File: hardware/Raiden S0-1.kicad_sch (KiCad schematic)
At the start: 42 parts, among them J1 Conn_01x15, J2 Conn_01x15, J4 Conn_02x03_Counter_Clockwise, J5 Conn_02x02_Counter_Clockwise, J6 Conn_02x02_Counter_Clockwise, P1 USB_C_Receptacle_USB2.0_14P, SW1 SW_Push, SW2 SW_Push, U1 ESP32-S3FN8, U2 AZ1117C-3.3, Y1 32.768kHz, Y2 40MHz

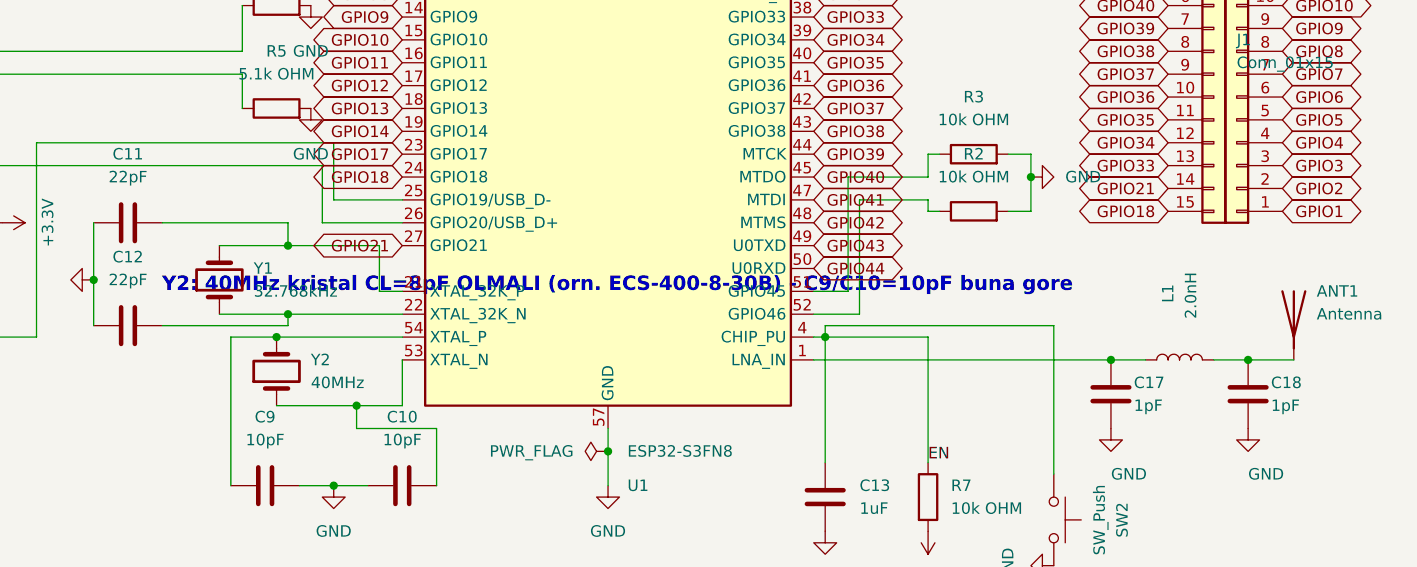
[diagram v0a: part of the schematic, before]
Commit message: Remove the Turkish crystal note from the schematic canvas
It overlapped the 32.768 kHz crystal label and was the only non-English text
on the sheet. The CL = 8 pF requirement is still recorded in README.md, the
BOM part number and fab/README.txt. ERC 0 violations; netlist verified
node-for-node identical.
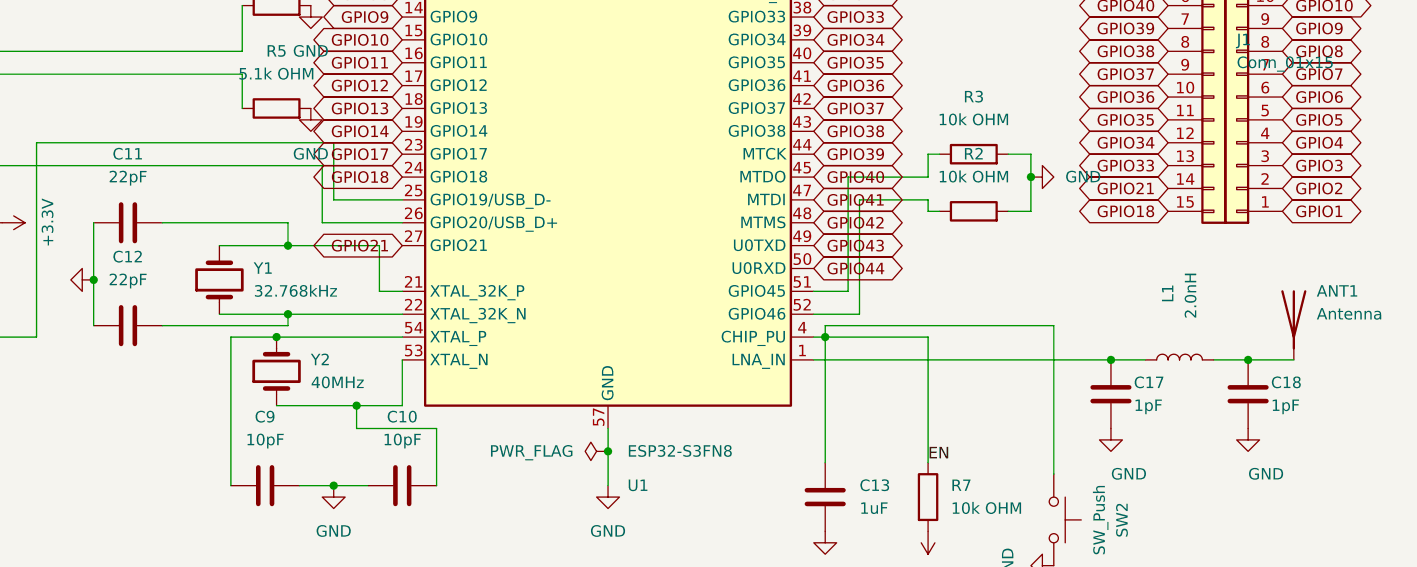
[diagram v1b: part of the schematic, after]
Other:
- note removed: "Y2: 40MHz kristal CL=8pF OLMALI (orn. ECS-400-8-30B) - C9/C10=10pF buna gore"
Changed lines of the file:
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@@
 	)
 	(embedded_fonts no)
-	(text "Y2: 40MHz kristal CL=8pF OLMALI (orn. ECS-400-8-30B) - C9/C10=10pF buna gore"
-		(exclude_from_sim no)
-		(at 240 220 0)
-		(effects
-			(font
-				(size 1.6 1.6)
-				(bold yes)
-			)
-			(justify left bottom)
-		)
-	)
 )
